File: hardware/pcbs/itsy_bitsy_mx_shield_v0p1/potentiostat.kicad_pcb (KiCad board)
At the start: 2 copper layers, 144.8 x 88.9 mm, 141 parts, among them K1 Conn_01x03, P1 Conn_01x02, P10 Conn_01x02, P11 Conn_01x02, P12 Conn_01x02, P13 Conn_02x05_Odd_Even, P14 Conn_02x05_Odd_Even, P15 Conn_02x02_Odd_Even, P16 Conn_02x02_Odd_Even, P17 Conn_01x02, P18 Conn_01x02, P19 Conn_01x02, P2 Conn_01x02, P20 Conn_01x02, P21 Conn_01x02, P22 Conn_01x02, P3 Conn_01x02, P4 Conn_01x02, P5 Conn_01x02, P6 Conn_01x02, P7 Conn_01x02, P8 Conn_01x02, P9 Conn_01x02, U1 74HC138, U10 REF33XX, U11 OP07, U12 OP07, U13 OP07, U14 OP07, U15 OP07, U16 OP07, U17 OP07, U18 OP07, U19 74HC138, U2 ITSY_BITSY_MX, U20 OP07, U21 74HC138, U3 DG411xY, U4 DG411xY, U5 DG411xY, U6 MEA1D05XXSC, U7 DG411xY, U8 DG411xY, U9 TL072

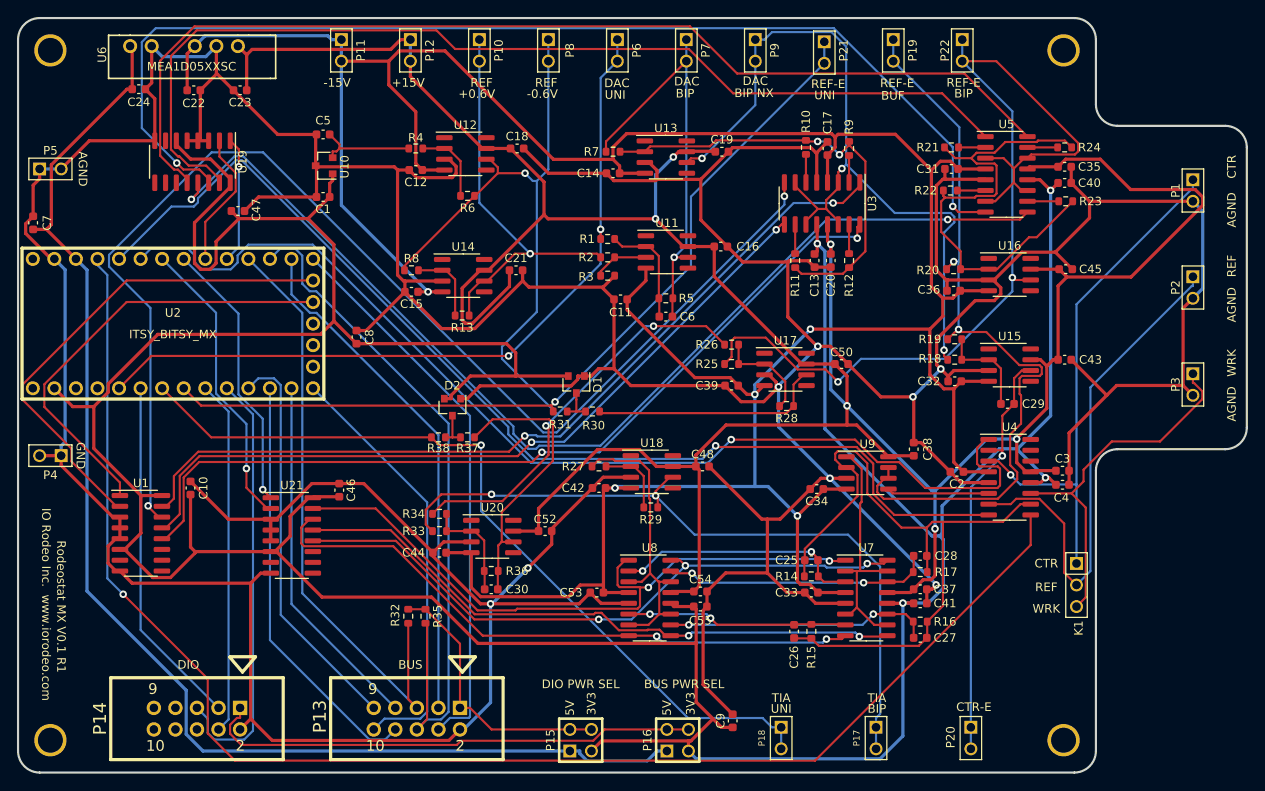
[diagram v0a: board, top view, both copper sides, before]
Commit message: Re-routed board and remade gerber files.
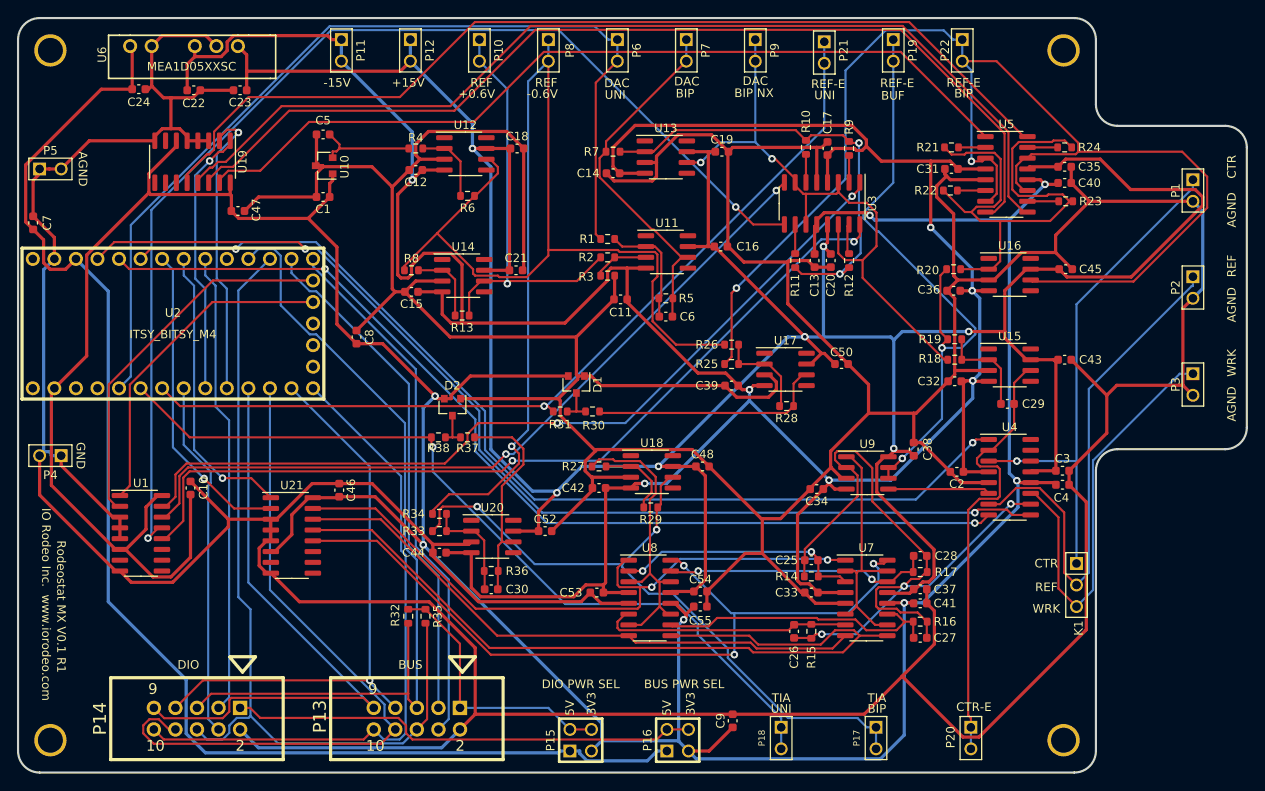
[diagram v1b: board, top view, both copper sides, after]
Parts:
- U2: value ITSY_BITSY_MX -> ITSY_BITSY_M4
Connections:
- P14 pad 10: Net-(P14-Pad10) -> /CS
- P14 pad 3: /A1_D15 -> /D7
- P14 pad 4: /A4_D18 -> /A3_D17
- P14 pad 5: /A5_D19 -> /SCL
- P14 pad 6: Net-(P14-Pad6) -> /SDA
- P14 pad 7: Net-(P14-Pad7) -> /POCI
- P14 pad 8: Net-(P14-Pad8) -> /PICO
- P14 pad 9: Net-(P14-Pad9) -> /SCK
- U2 pad 10: /A5_D19 -> /REF_GAIN_A1
- U2 pad 24: /REF_GAIN_A0 -> Net-(U2-Pad24)
- U2 pad 25: /REF_GAIN_A1 -> /D7
- U2 pad 6: /A1_D15 -> /TIA_OUT_UNI
- U2 pad 7: /TIA_OUT_UNI -> /REF_ELECT_UNI
- U2 pad 8: /REF_ELECT_UNI -> /A3_D17
- U2 pad 9: /A4_D18 -> /REF_GAIN_A0
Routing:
- net /GND: track 798.4 -> 893.8 mm, vias 8 -> 0
- net /D7: track 0.00 -> 54.6 mm
- net /SW_GAIN_2X: track 145.9 -> 91.6 mm
- net /A5_D19: track 51.2 -> 0.00 mm
- net /SW_WRK_ELECT: track 173.6 -> 127.1 mm, vias 1 -> 2
- net /SW_GAIN_5X: track 90.8 -> 133.8 mm
- net /3V3: track 454.2 -> 411.5 mm, vias 4 -> 7
- net /A3_D17: track 0.00 -> 42.1 mm
- net /A4_D18: track 41.8 -> 0.00 mm
- net /A1_D15: track 41.5 -> 0.00 mm
- net /REF_ELECT_BIP: track 116.1 -> 155.1 mm
- net /REF_NEG_0V6: track 119.5 -> 153.8 mm, vias 3 -> 1
- net /PICO: track 49.8 -> 82.8 mm
- net /SCL: track 71.5 -> 101.0 mm
- net /CS: track 50.8 -> 76.6 mm
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
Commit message: Fixed footprint issue with mx design.
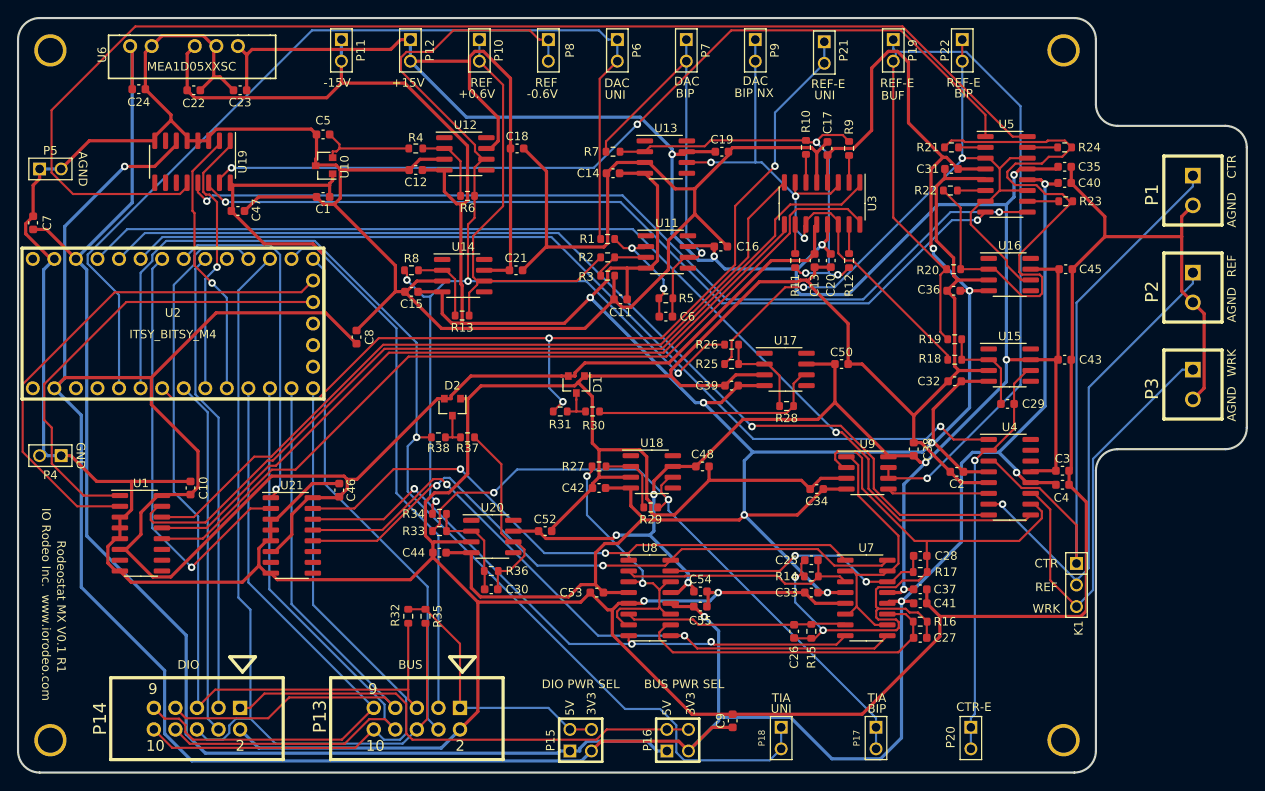
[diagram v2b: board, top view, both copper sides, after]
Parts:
- P1, P2, P3: footprint pin_array:PIN_ARRAY_2X1 -> ost_connblocks:CONNBLOCK2
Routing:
- net /3V3: track 411.5 -> 515.7 mm, vias 7 -> 5
- net /REF_ELECT_BIP: track 155.1 -> 83.8 mm
- net /SW_GAIN_5X: track 133.8 -> 88.7 mm, vias 2 -> 0
- net /TIA_OUT_UNI: track 98.2 -> 134.9 mm
- net /REF_ELECT_BUF: track 74.9 -> 110.5 mm, vias 2 -> 1
- net /SW_GAIN_INV_10X: track 114.3 -> 149.7 mm
- net /REF_NEG_0V6: track 153.8 -> 125.4 mm, vias 1 -> 4
- net /GND: track 893.8 -> 874.2 mm, vias 0 -> 2
- net /SW_TIA_GAIN_3: track 98.1 -> 80.7 mm, vias 0 -> 2
- net /-15V: track 366.5 -> 383.8 mm
- net /DAC_GAIN_A1: track 44.3 -> 61.4 mm
- net /SW_TIA_GAIN_4: track 93.0 -> 77.0 mm, vias 3 -> 2
- net /DAC_GAIN_A0: track 39.2 -> 55.0 mm
- net /SW_GAIN_INV_2X: track 117.3 -> 102.1 mm, vias 0 -> 2
- net /TIA_GAIN_A1: track 37.2 -> 50.9 mm
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
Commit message: Create gerbers for v0.1 r2 of the mx design.
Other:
- board text added: "Rodeostat MX V0.1 R2"
- board text removed: "Rodeostat MX V0.1 R1"

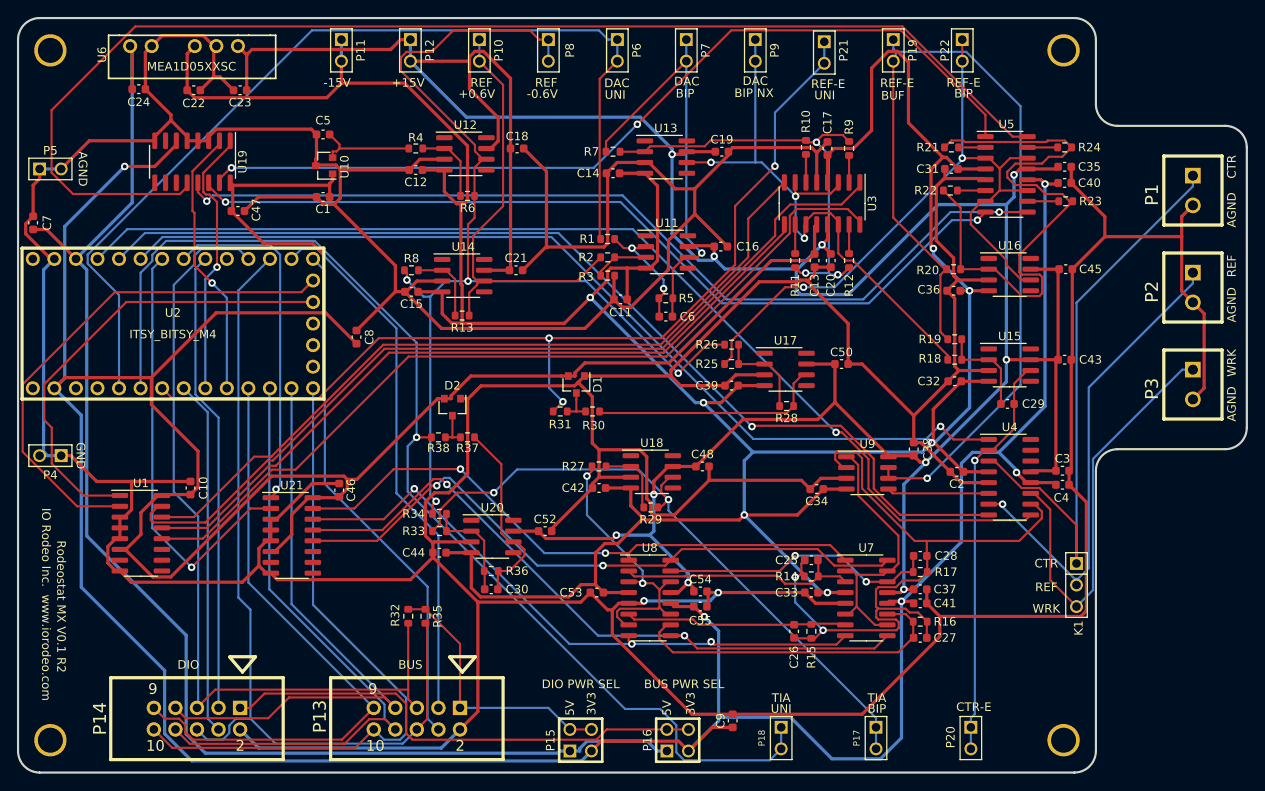
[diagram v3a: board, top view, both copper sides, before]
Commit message: Worked on layout, re-routing and BOM.
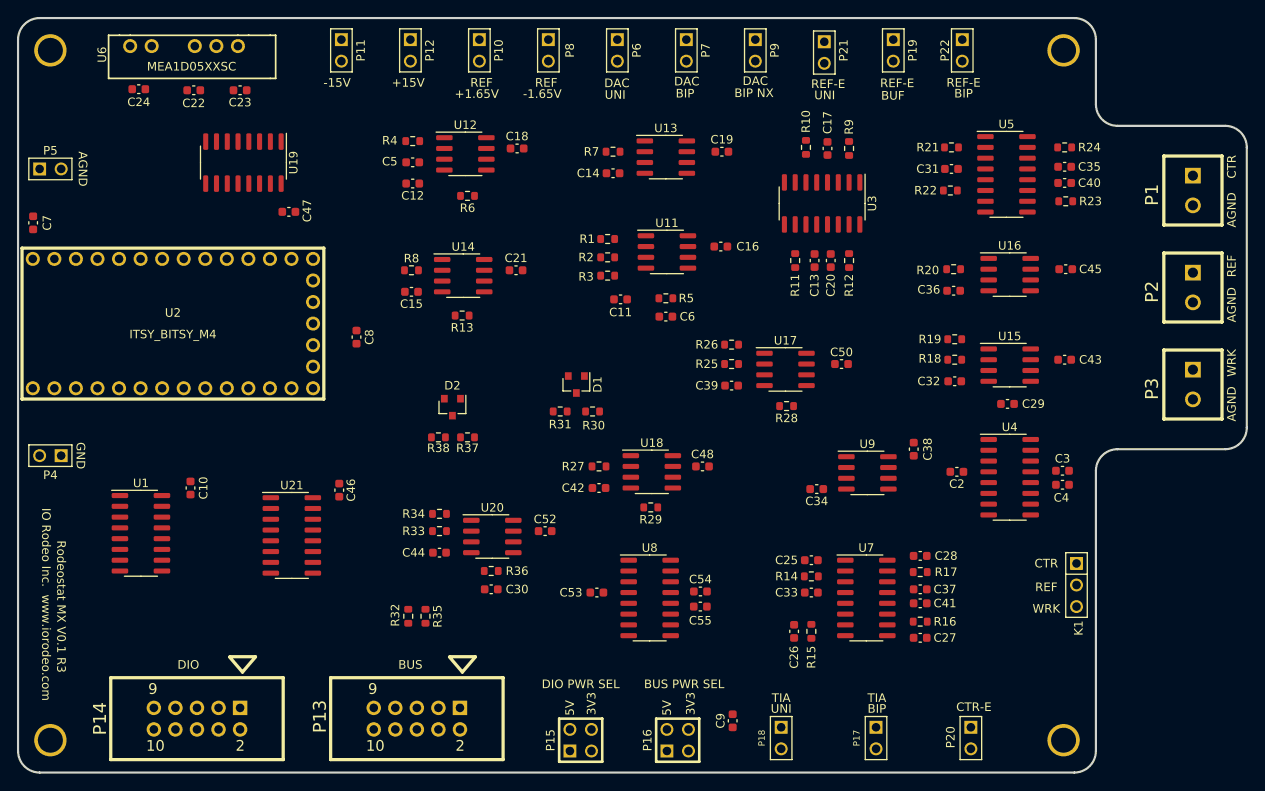
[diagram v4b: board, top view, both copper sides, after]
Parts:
- removed C1: 4.7uF, Capacitor_SMD:C_0603_1608Metric
- removed U10: REF33XX, Package_TO_SOT_SMD:SOT-23
- C25, C26, C27, C28: value 68nF -> 56nF
- R1, R2, R26, R28: value 12k -> 33k
- R14: value 300k -> 250k
- R15: value 30k -> 25k
- R16: value 3k -> 2.5k
- R17: value 300 -> 250
- R27: value 10k -> 5k
- R29: value 20k -> 33k
- R33, R34, R36: value 12k -> 10k
- R4: value 100k -> 20k
- R6: value 20k -> 10k
- moved C5 11.1 mm to (97.3, 67.8), turned to 0 degrees
- moved C47 6.00 mm to (82.7, 73.6)
- moved U19 6.00 mm to (77.4, 67.8)
- moved C12 1.63 mm to (97.3, 70.3)
- moved R4 0.94 mm to (97.3, 65.3)
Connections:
- net /REF_0V6 renamed /REF_1V65
- net /REF_NEG_0V6 renamed /REF_NEG_1V65
- C5 pad 1: /REF_3V -> /3V3
- R4 pad 2: /REF_3V -> /3V3
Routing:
- net /GND: track 874.2 -> 0.00 mm, vias 2 -> 0
- net /3V3: track 515.7 -> 0.00 mm, vias 5 -> 0
- net /-15V: track 383.8 -> 0.00 mm, vias 7 -> 0
- net /+15V: track 372.5 -> 0.00 mm, vias 10 -> 0
- net /5V: track 159.8 -> 0.00 mm
- net /SW_GAIN_INV_10X: track 149.7 -> 0.00 mm
- net /TIA_OUT_UNI: track 134.9 -> 0.00 mm, vias 1 -> 0
- net /SW_WRK_ELECT: track 127.9 -> 0.00 mm, vias 1 -> 0
- net /REF_NEG_1V65: track 125.4 -> 0.00 mm, vias 4 -> 0
- net /SW_REF_ELECT: track 119.6 -> 0.00 mm, vias 1 -> 0
- net /DAC_UNI: track 115.5 -> 0.00 mm
- net /REF_ELECT_UNI: track 114.9 -> 0.00 mm, vias 3 -> 0
- net /SW_CTR_ELECT: track 112.1 -> 0.00 mm, vias 1 -> 0
- net /REF_ELECT_BUF: track 110.5 -> 0.00 mm, vias 1 -> 0
- net /SW_GAIN_INV_5X: track 108.9 -> 0.00 mm, vias 2 -> 0
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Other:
- board text added: "+1.65V"
- board text added: "-1.65V"
- board text added: "Rodeostat MX V0.1 R3"
- board text removed: "+0.6V"
- board text removed: "-0.6V"
- board text removed: "Rodeostat MX V0.1 R2"

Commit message: Finished re-route of PCB.
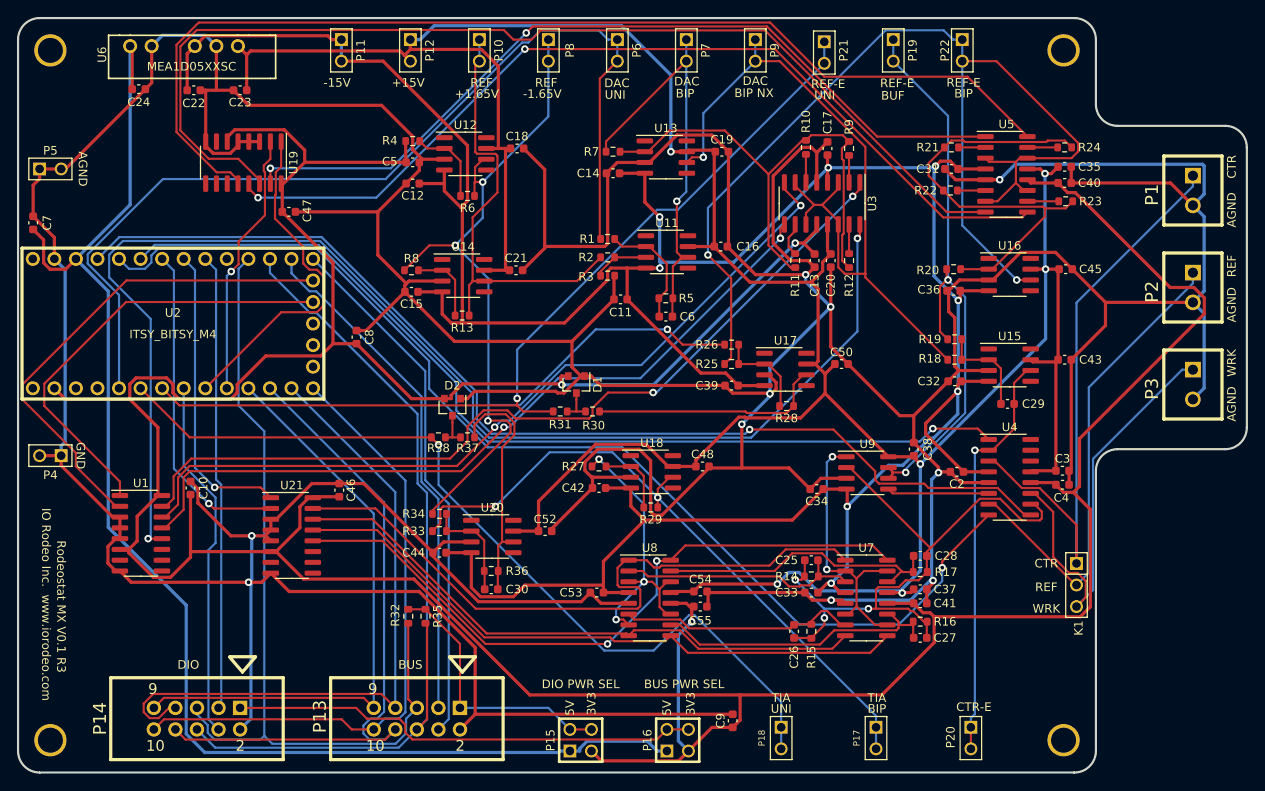
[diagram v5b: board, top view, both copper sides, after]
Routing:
- net /GND: track 0.00 -> 867.3 mm, vias 0 -> 10
- net /3V3: track 0.00 -> 460.6 mm, vias 0 -> 3
- net /+15V: track 0.00 -> 358.5 mm, vias 0 -> 6
- net /-15V: track 0.00 -> 354.0 mm, vias 0 -> 8
- net /5V: track 0.00 -> 162.1 mm
- net /SW_GAIN_10X: track 0.00 -> 155.5 mm, vias 0 -> 2
- net /SW_REF_ELECT: track 0.00 -> 131.4 mm, vias 0 -> 1
- net /REF_ELECT_BIP: track 0.00 -> 130.5 mm, vias 0 -> 2
- net /SW_GAIN_INV_2X: track 0.00 -> 127.5 mm
- net /SW_WRK_ELECT: track 0.00 -> 127.4 mm, vias 0 -> 1
- net /SW_GAIN_INV_10X: track 0.00 -> 127.2 mm
- net /DAC_UNI: track 0.00 -> 115.5 mm
- net /REF_NEG_1V65: track 0.00 -> 113.8 mm, vias 0 -> 4
- net /SW_CTR_ELECT: track 0.00 -> 113.3 mm, vias 0 -> 1
- net /SW_GAIN_INV_5X: track 0.00 -> 108.5 mm, vias 0 -> 2
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
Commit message: Added gerber files for rodeostat mx V0.1 R3. Added fab files.
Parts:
- R14: value 250k -> 300k
- R15: value 25k -> 30k
- R16: value 2.5k -> 3k
- R17: value 250 -> 300
- R27: value 5k -> 2k
- R29: value 33k -> 11k
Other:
- board text added: "±1, 10, 100, 1000 μA"
